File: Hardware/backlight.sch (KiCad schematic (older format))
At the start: 22 parts, among them Q1 IRLML2060, Q2 IRLML2060, Q3 IRLML2060

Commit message: Complete new schematic
Added MAX232 and fixed test points on switches
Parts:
- TP5: footprint TestPoint:TestPoint_Pad_1.0x1.0mm -> TestPoint:TestPoint_THTPad_1.0x1.0mm_Drill0.5mm
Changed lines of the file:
@@
 F 0 "TP5" H 4358 2468 50  0000 L CNN
 F 1 "TestPoint" H 4358 2377 50  0000 L CNN
-F 2 "TestPoint:TestPoint_Pad_1.0x1.0mm" H 4500 2350 50  0001 C CNN
+F 2 "TestPoint:TestPoint_THTPad_1.0x1.0mm_Drill0.5mm" H 4500 2350 50  0001 C CNN
 F 3 "~" H 4500 2350 50  0001 C CNN
 	1    4300 2350

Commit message: Fix incorrect footprints
Fixed incorrect footprint for IRLML2060 and updated LED values to use CLVBA-FKA.
Also started deleting unneccessary test points
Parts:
- removed TP4, TP5: TestPoint, TestPoint:TestPoint_THTPad_1.0x1.0mm_Drill0.5mm, symbol Connector:TestPoint
- D1, D2, D3: footprint footprints:CLVBA-FKA-CAEDH8BBB7A363 -> footprints:SOL150P350X210-4N; symbol serial-mini:SMD-LED-RGB(4P-0606) -> serial-mini:CLVBA-FKA-CAEDH8BBB7A363
- Q1, Q2, Q3: symbol Device:Q_NMOS_GDS -> serial-mini:IRLML2060TRPbF
- R10, R11, R13: value 74 -> 100
- R12, R14, R16: value 130 -> 155
- R15, R18, R19: value 90 -> 100
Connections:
- net GND: now also Q1.2 (S), Q2.2 (S), Q3.2 (S); no longer Q1.3 (S), Q2.3 (S), Q3.3 (S)
- net 1.7V@57mA renamed 2V@60mA
- net 2V@60mA: now also Q1.3 (D), Q3.3 (D), R10.1, R11.1, R13.1, TP7.1; no longer Q3.2 (D)
- removed net 1.7V@69mA: Q1.2 (D), R10.1, R11.1, R13.1, TP7.1
- net 3V@69mA renamed 3.1V@60mA
- net 3.1V@60mA: now also Q2.3 (D); no longer Q2.2 (D)
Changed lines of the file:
@@
 $EndDescr
 $Comp
-L serial-mini:SMD-LED-RGB(4P-0606) D?
+L serial-mini:CLVBA-FKA-CAEDH8BBB7A363 D?
 U 1 1 5F5BD596
 P 6350 4700
@@
 F 0 "D3" H 6350 4335 50  0000 C CNN
 F 1 "LED" H 6350 4426 50  0001 C CNN
-F 2 "footprints:CLVBA-FKA-CAEDH8BBB7A363" H 6350 4700 50  0001 L BNN
+F 2 "footprints:SOL150P350X210-4N" H 6350 4700 50  0001 L BNN
 F 3 "http://www.kingbrightusa.com/images/catalog/SPEC/APTF1616SEEZGKQBKC.pdf" H 6350 4700 50  0001 L BNN
 F 4 "" H 6350 4700 50  0001 L BNN "Field4"
@@
 $EndComp
 $Comp
-L serial-mini:SMD-LED-RGB(4P-0606) D?
+L serial-mini:CLVBA-FKA-CAEDH8BBB7A363 D?
 U 1 1 5F5BD59D
 P 6350 3300
@@
 F 0 "D1" H 6350 2935 50  0000 C CNN
 F 1 "LED" H 6350 3026 50  0001 C CNN
-F 2 "footprints:CLVBA-FKA-CAEDH8BBB7A363" H 6350 3300 50  0001 L BNN
+F 2 "footprints:SOL150P350X210-4N" H 6350 3300 50  0001 L BNN
 F 3 "http://www.kingbrightusa.com/images/catalog/SPEC/APTF1616SEEZGKQBKC.pdf" H 6350 3300 50  0001 L BNN
 F 4 "" H 6350 3300 50  0001 L BNN "Field4"
@@
 $EndComp
 $Comp
-L Device:Q_NMOS_GDS Q?
+L serial-mini:IRLML2060TRPbF Q?
 U 1 1 5F5BD5A3
 P 5300 3300
@@
 AR Path="/5F577AC1/5F5BD5B3" Ref="R13"  Part="1"
 F 0 "R13" H 5900 3550 45  0001 C CNN
-F 1 "74" H 5900 3750 45  0000 C CNN
+F 1 "100" H 5900 3750 45  0000 C CNN
 F 2 "Resistor_SMD:R_0603_1608Metric_Pad1.05x0.95mm_HandSolder" H 5900 3800 20  0001 C CNN
 F 3 "" H 5900 3650 60  0001 C CNN
@@
 AR Path="/5F577AC1/5F5BD5C1" Ref="R11"  Part="1"
 F 0 "R11" H 5850 4250 45  0001 C CNN
-F 1 "74" H 5850 4450 45  0000 C CNN
+F 1 "100" H 5850 4450 45  0000 C CNN
 F 2 "Resistor_SMD:R_0603_1608Metric_Pad1.05x0.95mm_HandSolder" H 5850 4500 20  0001 C CNN
 F 3 "" H 5850 4350 60  0001 C CNN
@@
 Connection ~ 5600 3650
 $Comp
-L Device:Q_NMOS_GDS Q?
+L serial-mini:IRLML2060TRPbF Q?
 U 1 1 5F5BD5CC
 P 5300 4000
@@
 AR Path="/5F577AC1/5F5BD5D4" Ref="R12"  Part="1"
 F 0 "R12" H 5900 3150 45  0001 C CNN
-F 1 "130" H 5900 3350 45  0000 C CNN
+F 1 "155" H 5900 3350 45  0000 C CNN
 F 2 "Resistor_SMD:R_0603_1608Metric_Pad1.05x0.95mm_HandSolder" H 5900 3400 20  0001 C CNN
 F 3 "" H 5900 3250 60  0001 C CNN
@@
 AR Path="/5F577AC1/5F5BD5DF" Ref="R14"  Part="1"
 F 0 "R14" H 5900 3900 45  0001 C CNN
-F 1 "130" H 5900 4100 45  0000 C CNN
+F 1 "155" H 5900 4100 45  0000 C CNN
 F 2 "Resistor_SMD:R_0603_1608Metric_Pad1.05x0.95mm_HandSolder" H 5900 4150 20  0001 C CNN
 F 3 "" H 5900 4000 60  0001 C CNN
@@
 	5500 3750 5500 3800
 $Comp
-L serial-mini:SMD-LED-RGB(4P-0606) D?
+L serial-mini:CLVBA-FKA-CAEDH8BBB7A363 D?
 U 1 1 5F5BD5EB
 P 6350 4000
@@
 F 0 "D2" H 6350 3635 50  0000 C CNN
 F 1 "LED" H 6350 3726 50  0001 C CNN
-F 2 "footprints:CLVBA-FKA-CAEDH8BBB7A363" H 6350 4000 50  0001 L BNN
+F 2 "footprints:SOL150P350X210-4N" H 6350 4000 50  0001 L BNN
 F 3 "http://www.kingbrightusa.com/images/catalog/SPEC/APTF1616SEEZGKQBKC.pdf" H 6350 4000 50  0001 L BNN
 F 4 "" H 6350 4000 50  0001 L BNN "Field4"
@@
 AR Path="/5F577AC1/5F5BD5F2" Ref="R16"  Part="1"
 F 0 "R16" H 5900 4600 45  0001 C CNN
-F 1 "130" H 5900 4800 45  0000 C CNN
+F 1 "155" H 5900 4800 45  0000 C CNN
 F 2 "Resistor_SMD:R_0603_1608Metric_Pad1.05x0.95mm_HandSolder" H 5900 4850 20  0001 C CNN
 F 3 "" H 5900 4700 60  0001 C CNN
@@
 AR Path="/5F577AC1/5F5BD5FD" Ref="R19"  Part="1"
 F 0 "R19" H 5950 4900 45  0001 C CNN
-F 1 "90" H 5950 5100 45  0000 C CNN
+F 1 "100" H 5950 5100 45  0000 C CNN
 F 2 "Resistor_SMD:R_0603_1608Metric_Pad1.05x0.95mm_HandSolder" H 5950 5150 20  0001 C CNN
 F 3 "" H 5950 5000 60  0001 C CNN
@@
 AR Path="/5F577AC1/5F5BD605" Ref="R15"  Part="1"
 F 0 "R15" H 5900 4050 45  0001 C CNN
-F 1 "90" H 5900 4250 45  0000 C CNN
+F 1 "100" H 5900 4250 45  0000 C CNN
 F 2 "Resistor_SMD:R_0603_1608Metric_Pad1.05x0.95mm_HandSolder" H 5900 4300 20  0001 C CNN
 F 3 "" H 5900 4150 60  0001 C CNN
@@
 AR Path="/5F577AC1/5F5BD60E" Ref="R18"  Part="1"
 F 0 "R18" H 5950 3300 45  0001 C CNN
-F 1 "90" H 5950 3500 45  0000 C CNN
+F 1 "100" H 5950 3500 45  0000 C CNN
 F 2 "Resistor_SMD:R_0603_1608Metric_Pad1.05x0.95mm_HandSolder" H 5950 3550 20  0001 C CNN
 F 3 "" H 5950 3400 60  0001 C CNN
@@
 AR Path="/5F577AC1/5F5BD638" Ref="R10"  Part="1"
 F 0 "R10" H 5800 2750 45  0001 C CNN
-F 1 "74" H 5800 2950 45  0000 C CNN
+F 1 "100" H 5800 2950 45  0000 C CNN
 F 2 "Resistor_SMD:R_0603_1608Metric_Pad1.05x0.95mm_HandSolder" H 5800 3000 20  0001 C CNN
 F 3 "" H 5800 2850 60  0001 C CNN
@@
 $EndComp
 Text Label 5400 3050 2    50   ~ 0
-1.7V@69mA
+2V@60mA
 Text Label 5500 3800 2    50   ~ 0
-3V@69mA
+3.1V@60mA
 Text Label 5400 4500 2    50   ~ 0
-1.7V@57mA
-$Comp
-L Device:Q_NMOS_GDS Q?
+2V@60mA
+$Comp
+L serial-mini:IRLML2060TRPbF Q?
 U 1 1 5F5BD641
 P 5300 4700
@@
 Text HLabel 5100 4700 0    50   Input ~ 0
 Green
-$Comp
-L Connector:TestPoint TP?
-U 1 1 5F6BE002
-P 4300 2350
-AR Path="/5F6BE002" Ref="TP?"  Part="1"
-AR Path="/5F577AC1/5F6BE002" Ref="TP5"  Part="1"
-F 0 "TP5" H 4358 2468 50  0000 L CNN
-F 1 "TestPoint" H 4358 2377 50  0000 L CNN
-F 2 "TestPoint:TestPoint_THTPad_1.0x1.0mm_Drill0.5mm" H 4500 2350 50  0001 C CNN
-F 3 "~" H 4500 2350 50  0001 C CNN
-	1    4300 2350
-	1    0    0    -1
-$EndComp
 $Comp
 L serial-mini:3352T-1-103LF R?
@@
 Text HLabel 4700 2350 2    50   Input ~ 0
 Hue
-Connection ~ 4300 2350
 Wire Wire Line
 	4300 2350 4700 2350
@@
 	1    0    0    -1
 $EndComp
-Connection ~ 3900 3700
 Text HLabel 4250 3700 2    50   Input ~ 0
 Brightness
-$Comp
-L Connector:TestPoint TP?
-U 1 1 5F70CB1C
-P 3900 3700
-AR Path="/5F70CB1C" Ref="TP?"  Part="1"
-AR Path="/5F577AC1/5F70CB1C" Ref="TP4"  Part="1"
-F 0 "TP4" V 3854 3888 50  0000 L CNN
-F 1 "TestPoint" V 3945 3888 50  0000 L CNN
-F 2 "TestPoint:TestPoint_THTPad_1.0x1.0mm_Drill0.5mm" H 4100 3700 50  0001 C CNN
-F 3 "~" H 4100 3700 50  0001 C CNN
-	1    3900 3700
-	1    0    0    -1
-$EndComp
 $EndSCHEMATC

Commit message: Fix faulty debounce circuit
Used wrong value resistor/misplaced on each switch.
Also adjusted value of RC circuits for a time constant of 1 microsecond (was 1 millisecond before)
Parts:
- TP7, TP8, TP9: footprint TestPoint:TestPoint_THTPad_1.0x1.0mm_Drill0.5mm -> TestPoint:TestPoint_Pad_1.0x1.0mm
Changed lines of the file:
@@
 F 1 "LED" H 6350 4426 50  0001 C CNN
 F 2 "footprints:SOL150P350X210-4N" H 6350 4700 50  0001 L BNN
-F 3 "http://www.kingbrightusa.com/images/catalog/SPEC/APTF1616SEEZGKQBKC.pdf" H 6350 4700 50  0001 L BNN
+F 3 "https://www.cree.com/led-components/media/documents/CLVBAFKA.pdf" H 6350 4700 50  0001 L BNN
 F 4 "" H 6350 4700 50  0001 L BNN "Field4"
 	1    6350 4700
@@
 F 1 "LED" H 6350 3026 50  0001 C CNN
 F 2 "footprints:SOL150P350X210-4N" H 6350 3300 50  0001 L BNN
-F 3 "http://www.kingbrightusa.com/images/catalog/SPEC/APTF1616SEEZGKQBKC.pdf" H 6350 3300 50  0001 L BNN
+F 3 "https://www.cree.com/led-components/media/documents/CLVBAFKA.pdf" H 6350 3300 50  0001 L BNN
 F 4 "" H 6350 3300 50  0001 L BNN "Field4"
 	1    6350 3300
@@
 F 1 "LED" H 6350 3726 50  0001 C CNN
 F 2 "footprints:SOL150P350X210-4N" H 6350 4000 50  0001 L BNN
-F 3 "http://www.kingbrightusa.com/images/catalog/SPEC/APTF1616SEEZGKQBKC.pdf" H 6350 4000 50  0001 L BNN
+F 3 "https://www.cree.com/led-components/media/documents/CLVBAFKA.pdf" H 6350 4000 50  0001 L BNN
 F 4 "" H 6350 4000 50  0001 L BNN "Field4"
 	1    6350 4000
@@
 F 0 "TP9" V 5595 4572 50  0000 C CNN
 F 1 "TestPoint" V 5504 4572 50  0000 C CNN
-F 2 "TestPoint:TestPoint_THTPad_1.0x1.0mm_Drill0.5mm" H 5600 4500 50  0001 C CNN
+F 2 "TestPoint:TestPoint_Pad_1.0x1.0mm" H 5600 4500 50  0001 C CNN
 F 3 "~" H 5600 4500 50  0001 C CNN
 	1    5400 4500
@@
 F 0 "TP8" V 5595 3872 50  0000 C CNN
 F 1 "TestPoint" V 5504 3872 50  0000 C CNN
-F 2 "TestPoint:TestPoint_THTPad_1.0x1.0mm_Drill0.5mm" H 5600 3800 50  0001 C CNN
+F 2 "TestPoint:TestPoint_Pad_1.0x1.0mm" H 5600 3800 50  0001 C CNN
 F 3 "~" H 5600 3800 50  0001 C CNN
 	1    5400 3800
@@
 F 0 "TP7" V 5595 2922 50  0000 C CNN
 F 1 "TestPoint" V 5504 2922 50  0000 C CNN
-F 2 "TestPoint:TestPoint_THTPad_1.0x1.0mm_Drill0.5mm" H 5600 2850 50  0001 C CNN
+F 2 "TestPoint:TestPoint_Pad_1.0x1.0mm" H 5600 2850 50  0001 C CNN
 F 3 "~" H 5600 2850 50  0001 C CNN
 	1    5400 2850

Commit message: Add BOM
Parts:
- D1, D2, D3: value LED -> CLVBA-FKA
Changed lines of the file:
@@
 AR Path="/5F577AC1/5F5BD596" Ref="D3"  Part="1"
 F 0 "D3" H 6350 4335 50  0000 C CNN
-F 1 "LED" H 6350 4426 50  0001 C CNN
+F 1 "CLVBA-FKA" H 6350 4426 50  0001 C CNN
 F 2 "footprints:SOL150P350X210-4N" H 6350 4700 50  0001 L BNN
 F 3 "https://www.cree.com/led-components/media/documents/CLVBAFKA.pdf" H 6350 4700 50  0001 L BNN
@@
 AR Path="/5F577AC1/5F5BD59D" Ref="D1"  Part="1"
 F 0 "D1" H 6350 2935 50  0000 C CNN
-F 1 "LED" H 6350 3026 50  0001 C CNN
+F 1 "CLVBA-FKA" H 6350 3026 50  0001 C CNN
 F 2 "footprints:SOL150P350X210-4N" H 6350 3300 50  0001 L BNN
 F 3 "https://www.cree.com/led-components/media/documents/CLVBAFKA.pdf" H 6350 3300 50  0001 L BNN
@@
 AR Path="/5F577AC1/5F5BD5EB" Ref="D2"  Part="1"
 F 0 "D2" H 6350 3635 50  0000 C CNN
-F 1 "LED" H 6350 3726 50  0001 C CNN
+F 1 "CLVBA-FKA" H 6350 3726 50  0001 C CNN
 F 2 "footprints:SOL150P350X210-4N" H 6350 4000 50  0001 L BNN
 F 3 "https://www.cree.com/led-components/media/documents/CLVBAFKA.pdf" H 6350 4000 50  0001 L BNN

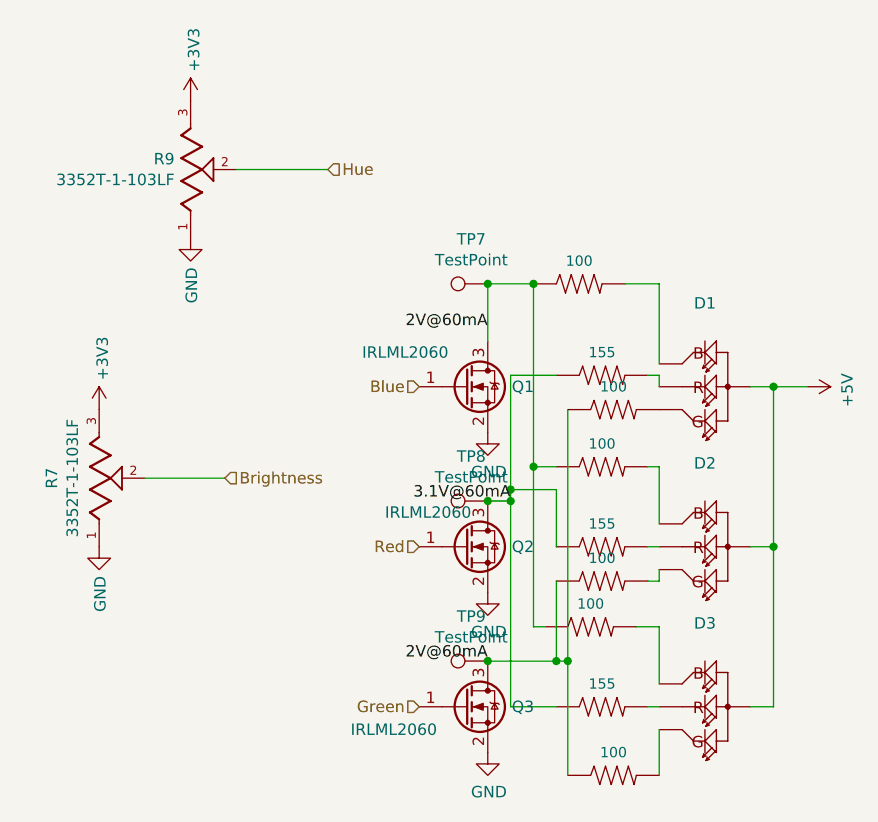
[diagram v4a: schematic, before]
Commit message: Fix PRTR5V0U2F footprint
Footprint was flipped wrong way on PCB, also removed BOM folder since it messed up Linguist
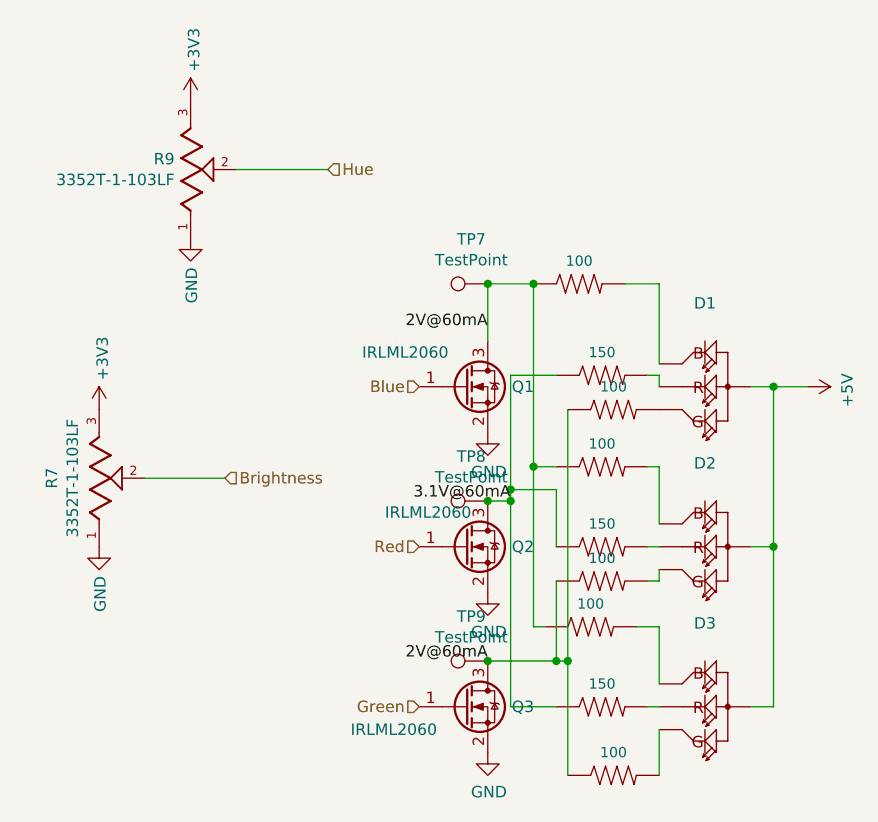
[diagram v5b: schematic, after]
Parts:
- R12, R14, R16: value 155 -> 150
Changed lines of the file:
@@
 AR Path="/5F577AC1/5F5BD5D4" Ref="R12"  Part="1"
 F 0 "R12" H 5900 3150 45  0001 C CNN
-F 1 "155" H 5900 3350 45  0000 C CNN
+F 1 "150" H 5900 3350 45  0000 C CNN
 F 2 "Resistor_SMD:R_0603_1608Metric_Pad1.05x0.95mm_HandSolder" H 5900 3400 20  0001 C CNN
 F 3 "" H 5900 3250 60  0001 C CNN
@@
 AR Path="/5F577AC1/5F5BD5DF" Ref="R14"  Part="1"
 F 0 "R14" H 5900 3900 45  0001 C CNN
-F 1 "155" H 5900 4100 45  0000 C CNN
+F 1 "150" H 5900 4100 45  0000 C CNN
 F 2 "Resistor_SMD:R_0603_1608Metric_Pad1.05x0.95mm_HandSolder" H 5900 4150 20  0001 C CNN
 F 3 "" H 5900 4000 60  0001 C CNN
@@
 AR Path="/5F577AC1/5F5BD5F2" Ref="R16"  Part="1"
 F 0 "R16" H 5900 4600 45  0001 C CNN
-F 1 "155" H 5900 4800 45  0000 C CNN
+F 1 "150" H 5900 4800 45  0000 C CNN
 F 2 "Resistor_SMD:R_0603_1608Metric_Pad1.05x0.95mm_HandSolder" H 5900 4850 20  0001 C CNN
 F 3 "" H 5900 4700 60  0001 C CNN
